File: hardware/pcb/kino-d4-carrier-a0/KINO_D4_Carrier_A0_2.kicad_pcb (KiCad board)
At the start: 4 copper layers, 117 x 69.4 mm, 250 parts, among them J100 P4 JP1 - 26 pin IDC, J1000 USB4105-GF-A, J101 C6 service - 3V3 sense only, J102 3V3 I2C accessory, J1100 PROTECTED 1S PACK / NTC, J1300 POWER PUSHBUTTON, J200 XIAO ESP32-S3 Sense socket, J201 GPIO breakout - SD/strap rest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, J300 XIAO ESP32-S3 Sense socket, J301 GPIO breakout - SD/strap rest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, J400 XIAO ESP32-S3 Sense socket, J401 GPIO breakout - SD/strap rest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, J500 XIAO ESP32-S3 Sense socket, J501 GPIO breakout - SD/strap rest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, J600 POGO TEST - SENSE ONLY, J601 EXTERNAL FLASH LOGIC, J800 3V PRIMARY RTC BACKUP, J900 HAPTIC MOTOR, J901 COVER HALL SENSOR, J902 LOCAL SHUTTER, J903 REMOTE DRY CONTACT, J904 FUNCTION BUTTON, Q1000 AO4407A, Q1001 AO4407A, Q1200 AO4407A, Q1201 AO4407A, Q1202 2N7002, Q1300 2N7002, Q900 2N7002, U100 TCA9517ADGKR, U1000 STUSB4500QTR, U1100 BQ25798RQMR, U1200 TPS61288LRQQR, U1201 TPS62162DSGR, U1300 LTC2955ITS8-1, U200 TXU0304PWR, U201 TPS2553DBVR, U300 TXU0304PWR, U301 TPS2553DBVR, U400 TXU0304PWR, U401 TPS2553DBVR, U500 TXU0304PWR, U501 TPS2553DBVR, U600 TCA9539PWR, U601 SN74LVC08APWR, U700 PAC1954T-E/4MX, U701 BQ27441DRZR-G1A, U800 LSM6DSOXTR, U801 RV-3028-C7, U802 TMP117AIDRVR, U900 DRV2605LDGSR, U901 SN74LVC1G14DBVR

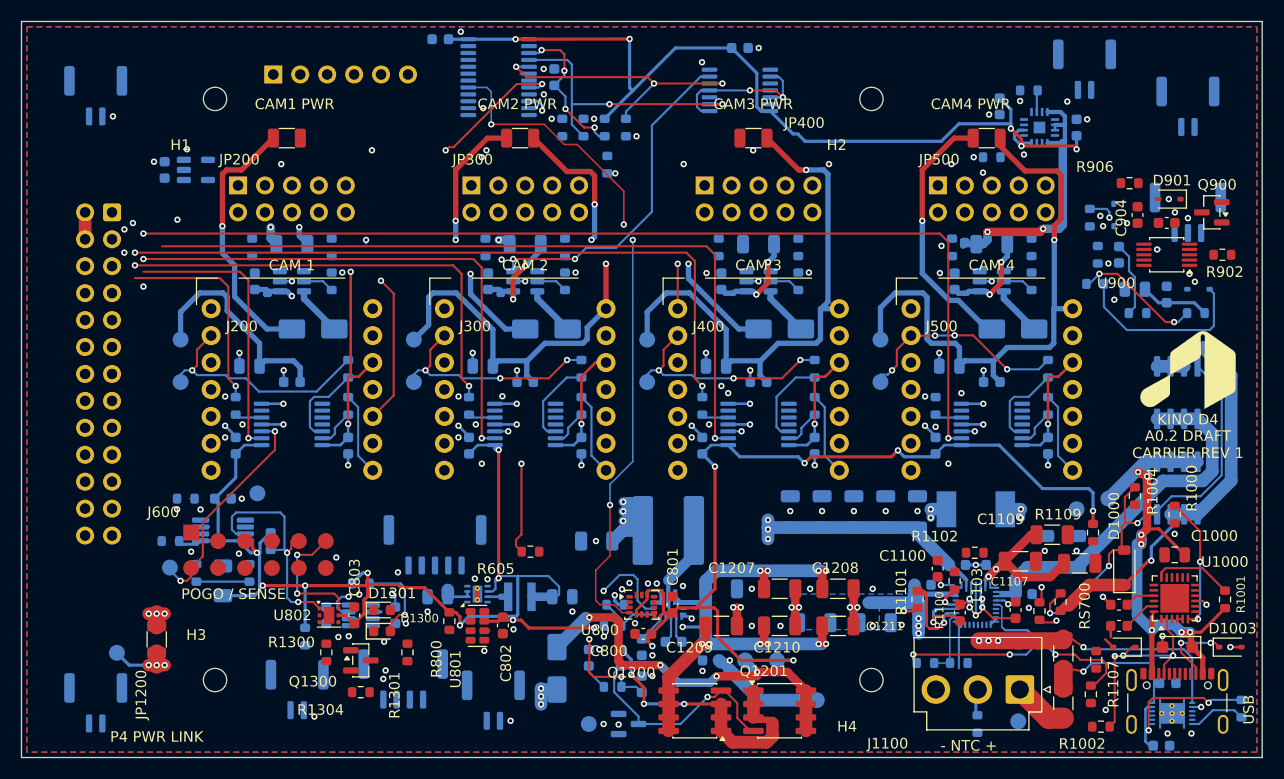
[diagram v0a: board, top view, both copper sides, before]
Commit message: feat(hardware): carrier A0.2 - SYS_5V camera supply routed as a tree
- 0.7 mm F trunk along y 19.4 over the four camera shunts (2.5 A at
  20 C rise); F because the P4 bus already walls that band, so In2 stays
  free for the header-to-socket GPIO.
- 2.0 mm In2 riser between cameras 2 and 3 (B hop under the SYNC bus),
  fed from Q1201 and, through a 1.4 mm In2 link replacing the 0.8 mm
  zig-zag, from D1200; three vias at every layer change.
- U1201 and J600 branches via the grid router; J600 straightened.
- U700 SENSE+ pins untied for separate Kelvin pairs (review P1).
- grid_router.py: GR_SKIP_REF leaves named parts for designed routes.

Co-Authored-By: Claude Opus 5.5 <noreply@anthropic.com>
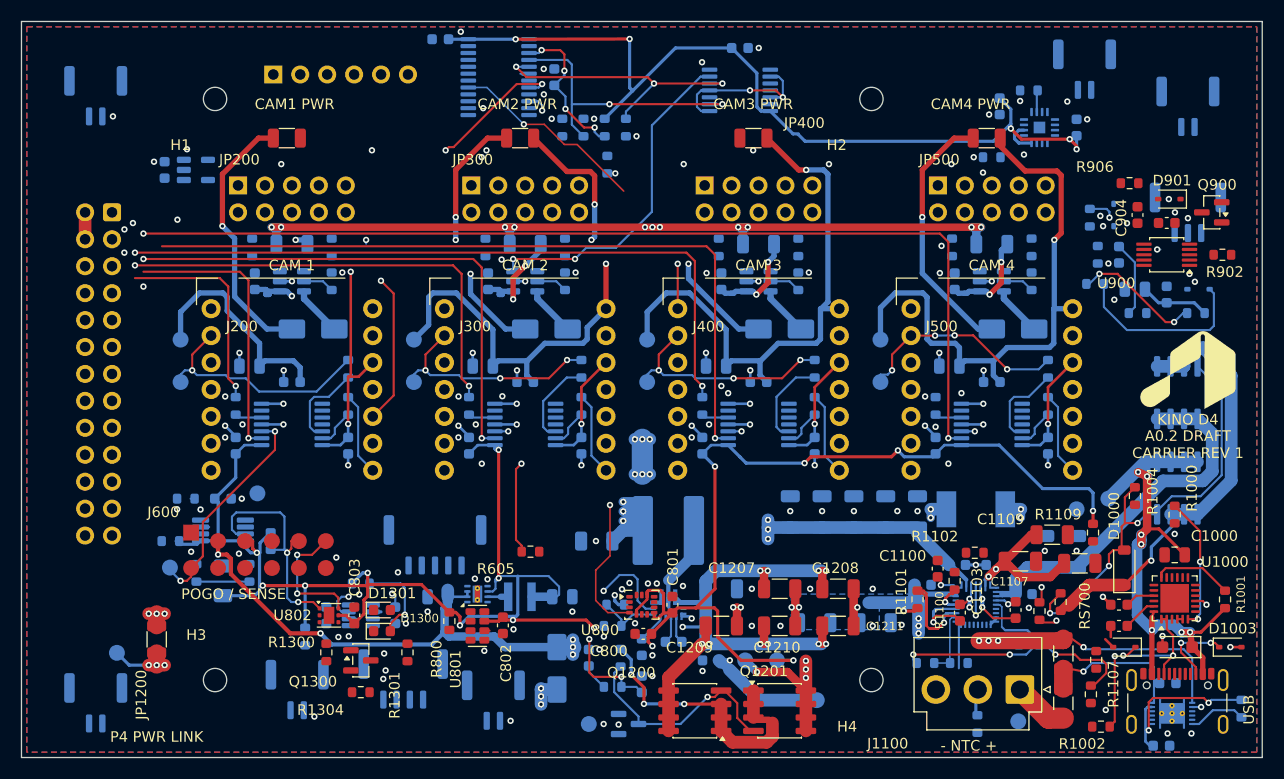
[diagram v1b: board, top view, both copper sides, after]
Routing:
- net SYS_5V: track 68.7 -> 236.2 mm, vias 8 -> 26
- net IMU_INT: track 64.6 -> 31.9 mm, vias 4 -> 2
- net CAM1_SHUNT_OUT: track 13.5 -> 11.8 mm
- net CAM3_3V3: track 11.3 -> 10.8 mm
- net CAM2_3V3: track 11.3 -> 10.8 mm
- net CAM4_3V3: track 11.3 -> 10.8 mm
- net GND: vias 151 -> 150

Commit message: feat(hardware): carrier A0.2 - signal routing pass, 195 -> 114 open
Grid router over every open net except the camera header-to-socket
GPIO (handled next as a per-camera template), leaving U700's Kelvin pins
for designed pairs; tidy pass afterwards. No clearance or short
violations; six routes at minimum clearance are listed in the README for
review. The router now lets through-hole pads exit at 45 degrees as well
as on their centre lines (header first rows escape between second-row
pins); SMD pads keep the strict ODD JOBS 87/88 entry.

Co-Authored-By: Claude Opus 5.5 <noreply@anthropic.com>
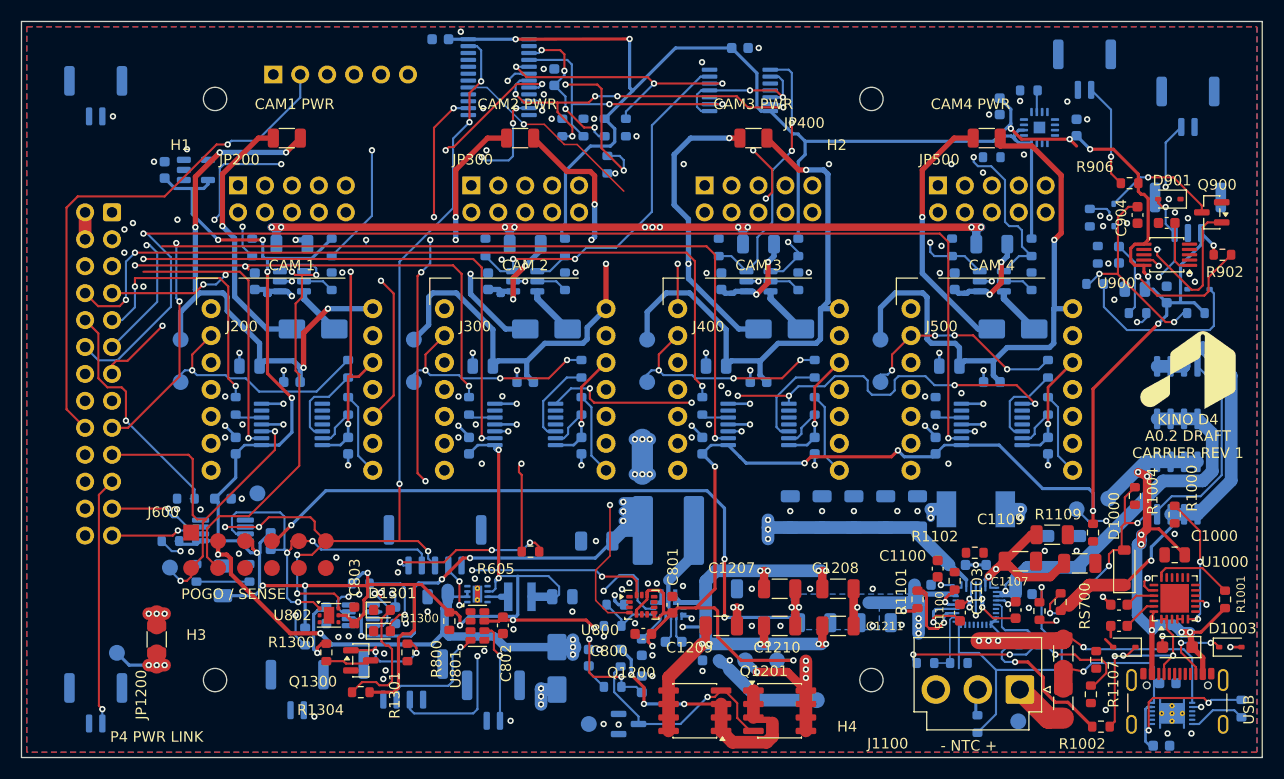
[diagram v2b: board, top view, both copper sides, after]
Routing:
- net MB_3V3: track 300.3 -> 446.3 mm, vias 20 -> 27
- net I2C_SDA: track 11.9 -> 135.4 mm, vias 2 -> 12
- net POWER_INT_N: track 0.00 -> 68.3 mm, vias 0 -> 8
- net CAM1_EN: track 38.0 -> 103.4 mm, vias 2 -> 6
- net BAT_PROTECTED: track 48.0 -> 110.9 mm, vias 8 -> 11
- net P4_BUS_EN: track 5.00 -> 58.6 mm, vias 0 -> 6
- net C6_3V3_TEST: track 0.00 -> 50.0 mm, vias 0 -> 1
- net SYS_RAW: track 75.6 -> 120.2 mm, vias 8 -> 12
- net CAM4_REQ: track 0.00 -> 34.6 mm, vias 0 -> 5
- net SHUTTER_N: track 0.00 -> 34.5 mm, vias 0 -> 2
- net CAM1_5V: track 21.3 -> 54.9 mm, vias 0 -> 5
- net CAM3_EN: track 0.00 -> 25.8 mm, vias 0 -> 2
- net CHG_TS: track 6.01 -> 31.4 mm
- net CAM4_FAULT_N: track 46.4 -> 71.5 mm, vias 2 -> 4
- net CHG_VBUS: track 37.2 -> 62.2 mm, vias 0 -> 2
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
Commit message: feat(hardware): carrier A0.2 - camera GPIO breakout as one In2 fan-out per camera
route_a02_cam_gpio.py lays the eight header-to-socket GPIO lines of each
camera as the same template: row-2 header pins straight down, row-1 pins
at 45 degrees into the gap beside them, eight 1.27 mm In2 lanes, each
turning 45 degrees at its socket pin's depth (left column D0-D5 nested
shallowest-first, right column D8-D10 deepest-innermost), so nothing
crosses. Before the lanes go in it relocates GND stitching vias, moves
the SYS_5V drop via and two per-camera GND vias to lane midpoints, and
removes the unlocked router copper in the way for re-routing.
Unconnected 133 -> 101 before that re-route.

Co-Authored-By: Claude Opus 5.5 <noreply@anthropic.com>
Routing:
- net P4_BUS_EN: track 58.6 -> 14.8 mm, vias 6 -> 0
- net CAM4_D5: track 0.00 -> 29.2 mm
- net CAM3_D5: track 0.00 -> 29.2 mm
- net CAM2_D5: track 0.00 -> 29.2 mm
- net CAM1_D5: track 0.00 -> 29.2 mm
- net MB_3V3: track 446.3 -> 417.3 mm, vias 27 -> 23
- net CAM4_D9_SD: track 0.00 -> 24.7 mm
- net CAM3_D9_SD: track 0.00 -> 24.7 mm
- net CAM2_D9_SD: track 0.00 -> 24.7 mm
- net CAM4_D8_SD: track 0.00 -> 24.7 mm
- net CAM3_D8_SD: track 0.00 -> 24.7 mm
- net CAM2_D8_SD: track 0.00 -> 24.7 mm
- net CAM1_D8_SD: track 0.00 -> 24.7 mm
- net CAM4_D4: track 0.00 -> 23.0 mm
- net CAM3_D4: track 0.00 -> 23.0 mm
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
